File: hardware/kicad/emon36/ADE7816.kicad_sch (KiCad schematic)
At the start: 39 parts, among them J2 MJ-3523-SMT, J3 MJ-3523-SMT, J4 MJ-3523-SMT, J5 MJ-3523-SMT, J6 MJ-3523-SMT

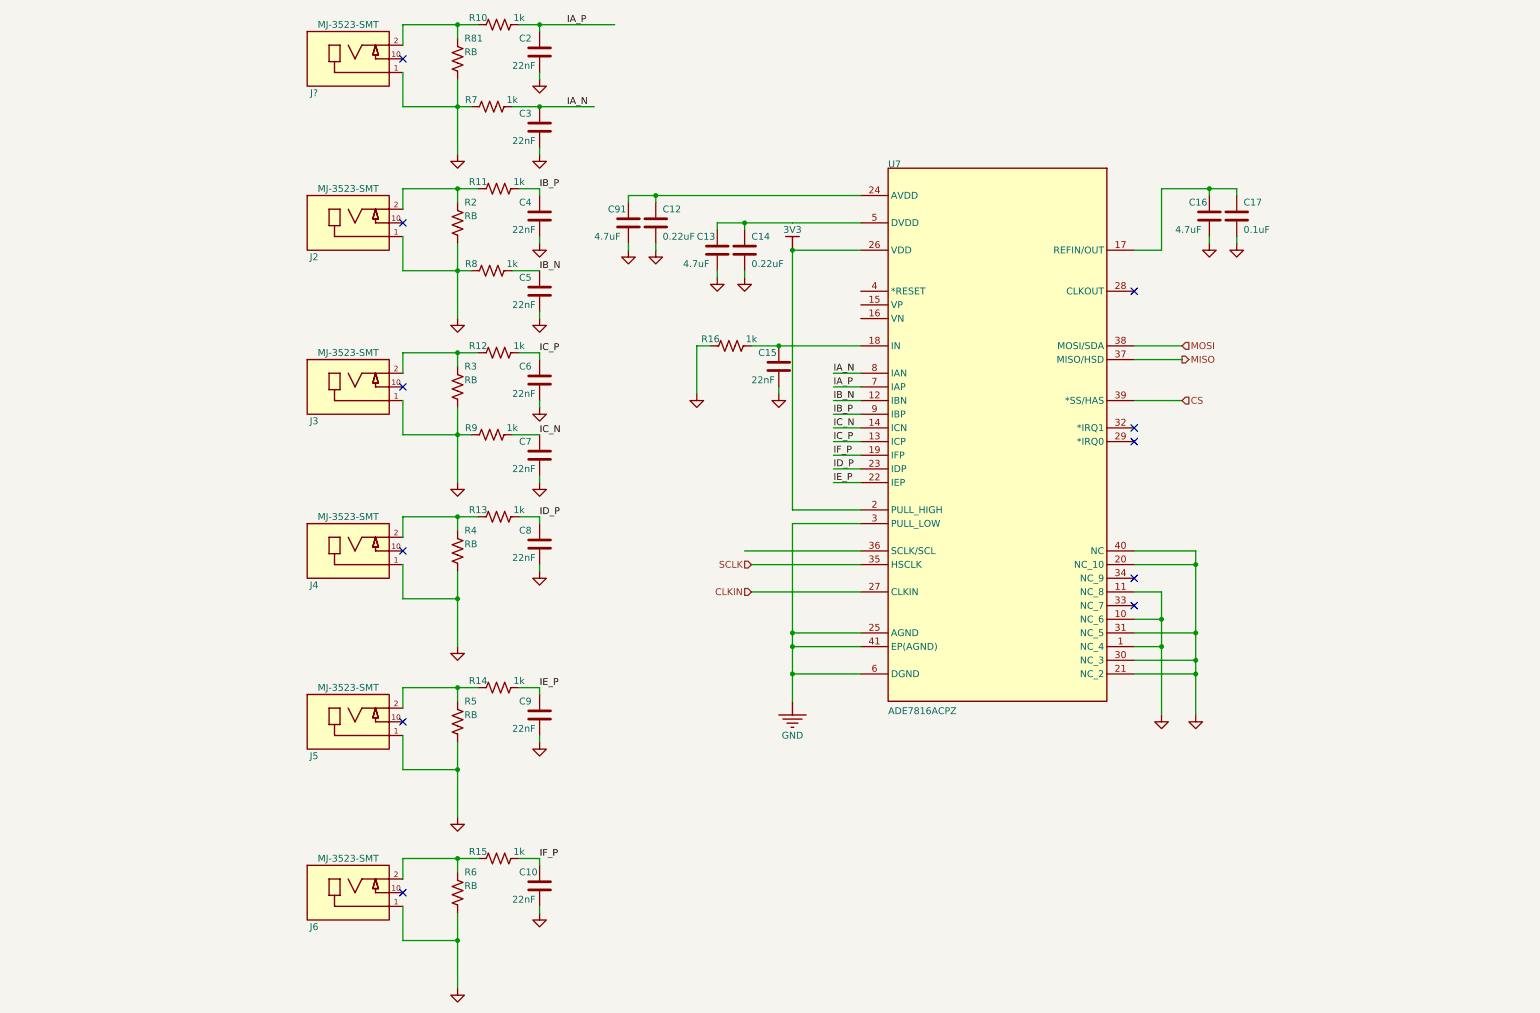
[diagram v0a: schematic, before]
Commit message: Add preliminary USB interface
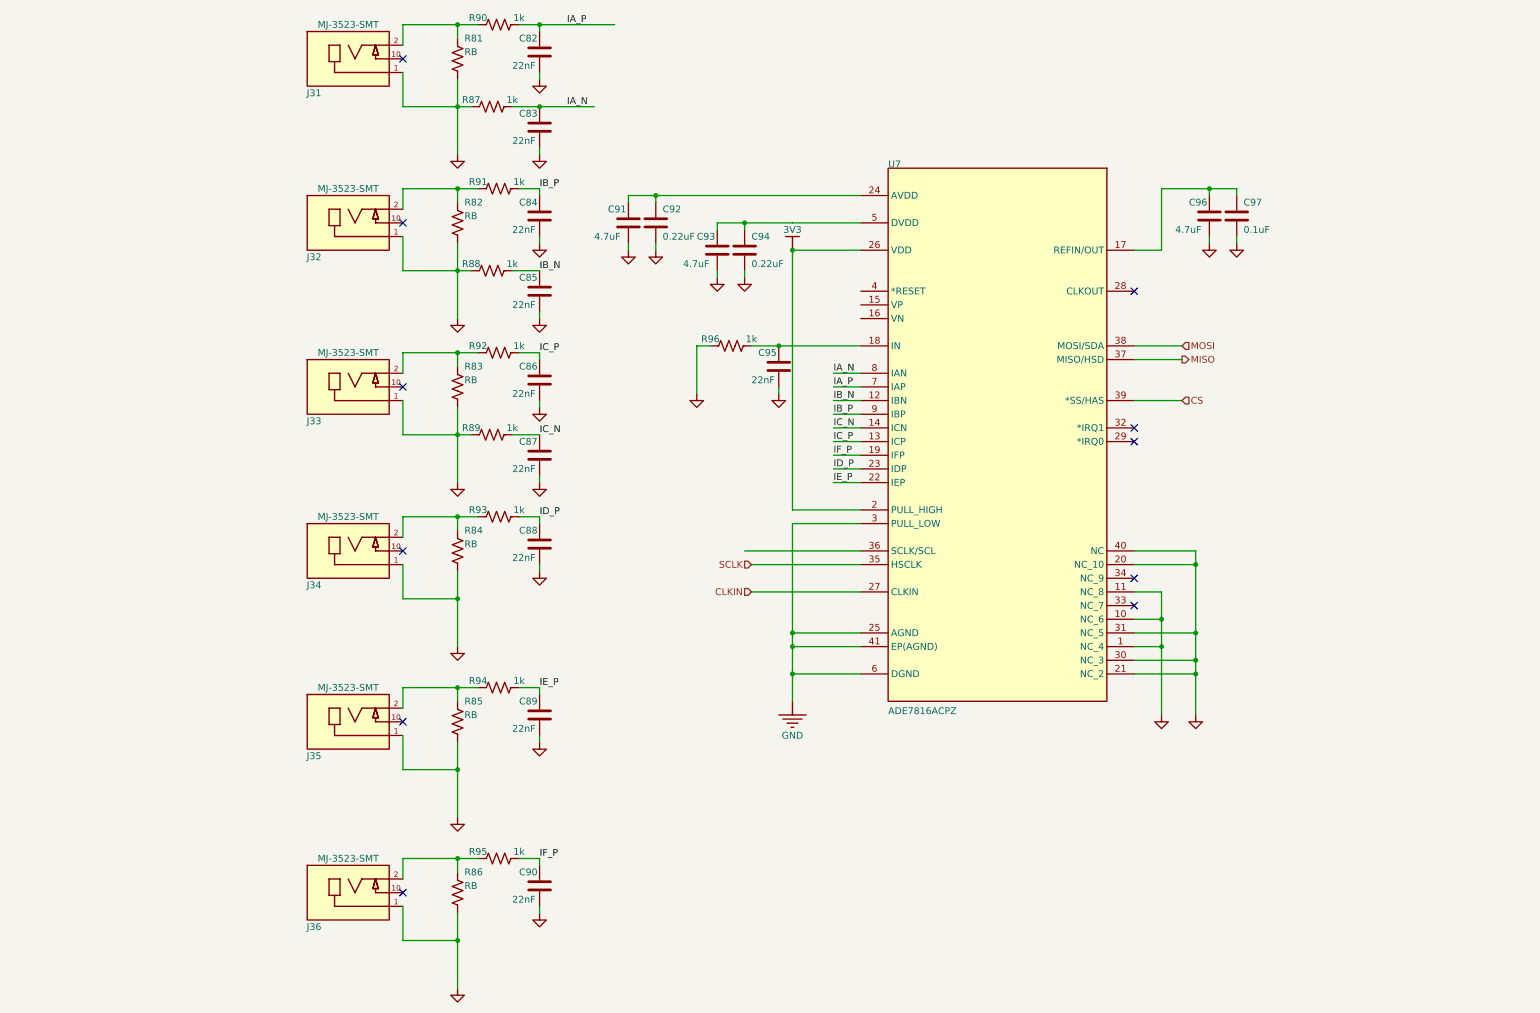
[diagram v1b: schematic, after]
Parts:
- C91: footprint (none) -> Capacitor_SMD:C_0603_1608Metric
- J31: renamed from J?; footprint CUI_MJ-3523-SMT -> emon36:CUI_MJ-3523-SMT
- J32: renamed from J2; footprint CUI_MJ-3523-SMT -> emon36:CUI_MJ-3523-SMT
- J33: renamed from J3; footprint CUI_MJ-3523-SMT -> emon36:CUI_MJ-3523-SMT
- J34: renamed from J4; footprint CUI_MJ-3523-SMT -> emon36:CUI_MJ-3523-SMT
- J35: renamed from J5; footprint CUI_MJ-3523-SMT -> emon36:CUI_MJ-3523-SMT
- J36: renamed from J6; footprint CUI_MJ-3523-SMT -> emon36:CUI_MJ-3523-SMT
- U7: footprint QFN50P600X600X75-41N-D -> emon36:QFN50P600X600X75-41N-D
- renumbered C2 to C82, C3 to C83, C4 to C84, C5 to C85, C6 to C86, C7 to C87, C8 to C88, C9 to C89, C10 to C90, C12 to C92, C13 to C93, C14 to C94, C15 to C95, C16 to C96, C17 to C97, R2 to R82, R3 to R83, R4 to R84, R5 to R85, R6 to R86, R7 to R87, R8 to R88, R9 to R89, R10 to R90, R11 to R91, R12 to R92, R13 to R93, R14 to R94, R15 to R95, R16 to R96

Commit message: Reverted to stacked 3.5mm connectors. Now has 42 channels. Added OLED, switches, power system. Cleaned up channel page.
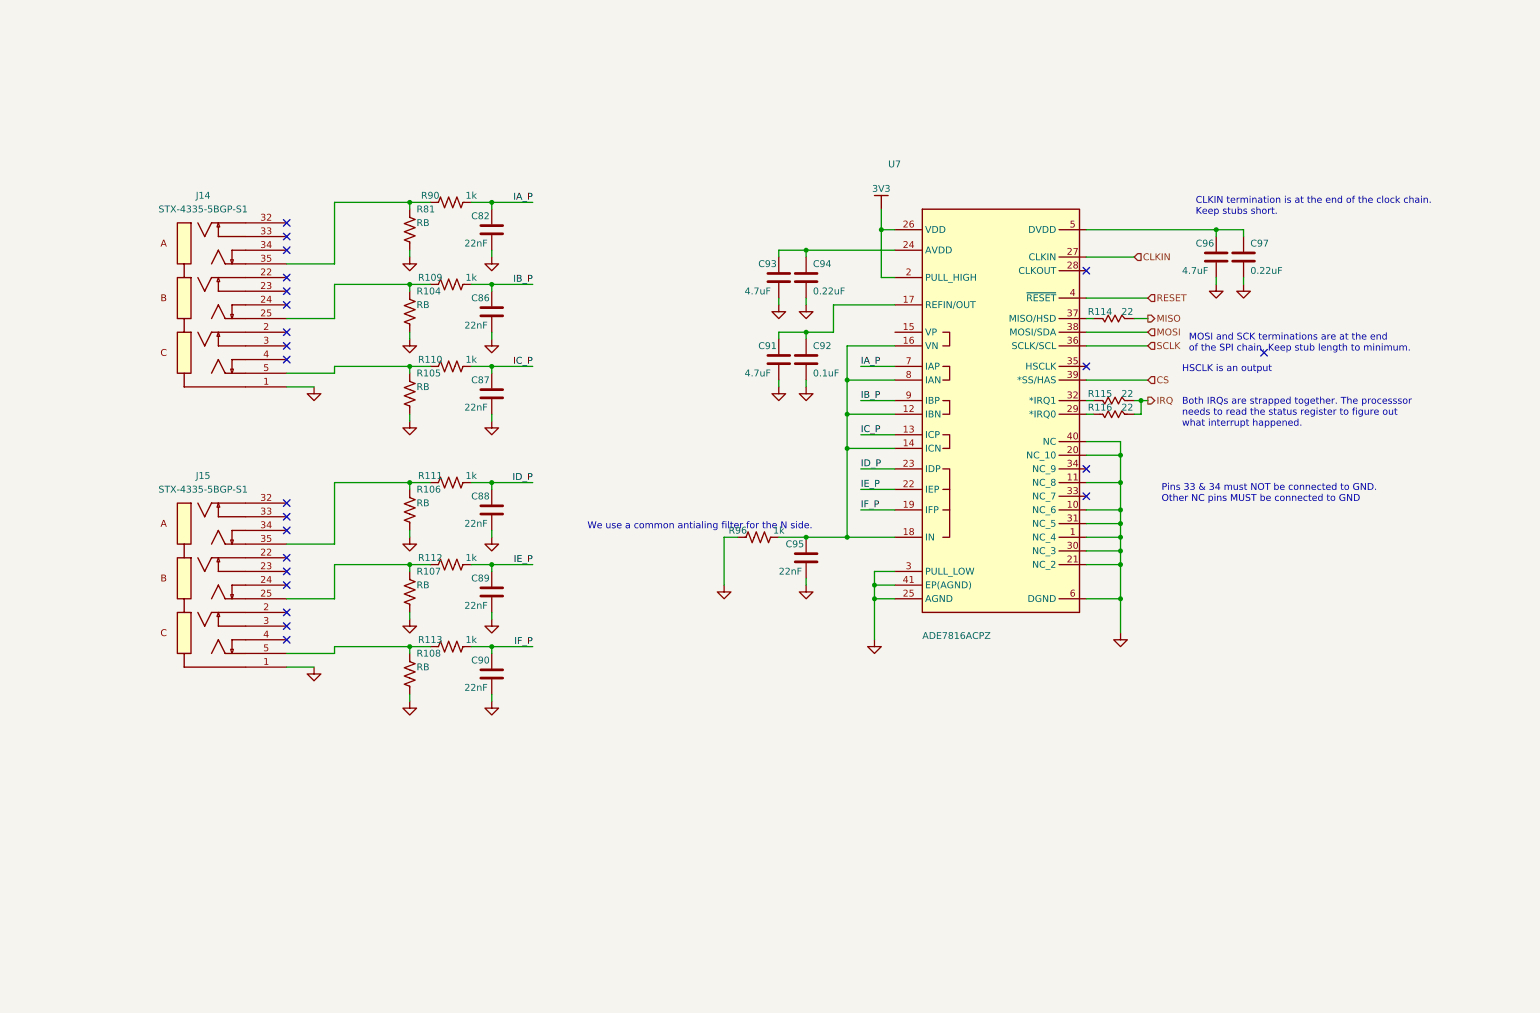
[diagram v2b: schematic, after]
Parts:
- removed C83, C84, C85: 22nF, Capacitor_SMD:C_0603_1608Metric, symbol Device:C
- removed J31, J32, J33, J34, J35, J36: MJ-3523-SMT, emon36:CUI_MJ-3523-SMT, symbol emon36:MJ-3523-SMT
- removed R82, R83, R84, R85, R86: RB, Resistor_SMD:R_0603_1608Metric, symbol Device:R_US
- removed R87, R88, R89, R91, R92, R93, R94, R95: 1k, Resistor_SMD:R_0603_1608Metric, symbol Device:R_US
- added J14, J15: STX-4335-5BGP-S1, Connector_Audio:STX-4335-5BGP-S1_KYC, symbol emon36:STX-4335-5BGP-S1
- added R104, R105, R106, R107, R108: RB, Resistor_SMD:R_0603_1608Metric, symbol Device:R_US
- added R109, R110, R111, R112, R113: 1k, Resistor_SMD:R_0603_1608Metric, symbol Device:R_US
- added R114, R115, R116: 22, Resistor_SMD:R_0603_1608Metric, symbol emon36:RES0603
- C92: value 0.22uF -> 0.1uF
- C97: value 0.1uF -> 0.22uF
- U7: symbol ADE7816-altium-import:0_ADE7816ACPZ -> emon36:ADE7816ACPZ
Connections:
- net IA_N is gone; now on an unnamed net: U7.8 (IAN)
- net IB_N is gone; now on an unnamed net: U7.12 (IBN)
- net GND: now also J14.1, J15.1, R104.2, R105.2, R106.2, R107.2, R108.2
- net IB_P: now also C86.1, R109.2
- net IC_P: now also C87.1, R110.2; no longer C86.1
- net ID_P: now also R111.2
- net IE_P: now also R112.2
- net IF_P: now also R113.2
- net MISO: now also R114.2; no longer U7.37 (MISO/HSD)
- net SCLK: now also U7.36 (SCLK/SCL); no longer U7.35 (HSCLK)
- net at C93.1, C94.1: now also U7.24 (AVDD); no longer U7.5 (DVDD)
- net at C91.1, C92.1: now also U7.17 (REFIN/OUT); no longer U7.24 (AVDD)
- net at R81.1, R90.1: now also J14.35
- net at C96.1, C97.1: now also U7.5 (DVDD); no longer U7.17 (REFIN/OUT)
- net at C95.1, R96.2, U7.18 (IN): now also U7.14 (ICN), U7.16 (VN)
- net at U7.29 (*IRQ0): now also R116.1
- net at U7.32 (*IRQ1): now also R115.1
- net RESET: now reaches U7.4 (~{RESET})
- removed net IC_N: C87.1, U7.14 (ICN)
- new net: J15.35, R106.1, R111.1
- new net: J15.25, R107.1, R112.1
- new net: J15.5, R108.1, R113.1
- new net: R114.1, U7.37 (MISO/HSD)
- new net: J14.25, R104.1, R109.1
- new net: J14.5, R105.1, R110.1
- new net IRQ: R115.2, R116.2
- no-connect marks 11 -> 23
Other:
- note added: "Both IRQs are strapped together. The processsor needs to read the status register to figure out what interrupt happened."
- note added: "CLKIN termination is at the end of the clock chain. Keep stubs short."
- note added: "HSCLK is an output"
- note added: "MOSI and SCK terminations are at the end of the SPI chain. Keep stub length to minimum."
- note added: "Pins 33 & 34 must NOT be connected to GND. Other NC pins MUST be connected to GND"
- note added: "We use a common antialing filter for the N side."
- moved on the sheet: C82, C93, C94, C95, R81, R90, R96

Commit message: Another major schematics/PCB iteration. Added decoupling caps, interrupts, etc. Improved power system. Added clock.
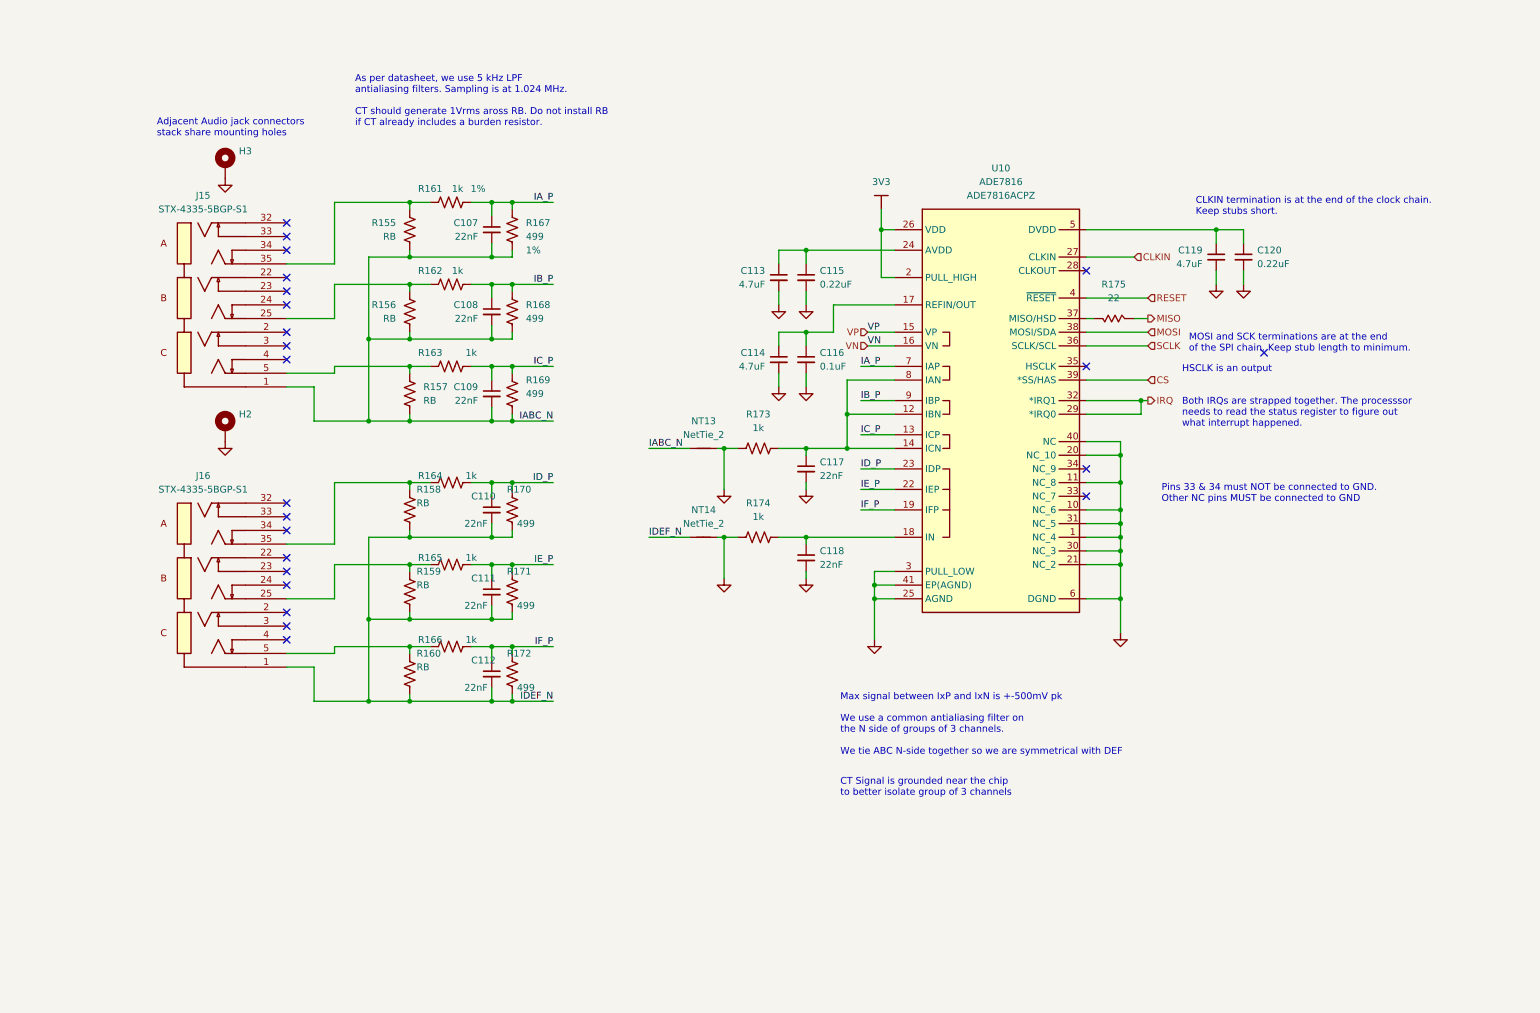
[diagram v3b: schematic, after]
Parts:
- removed R115, R116: 22, Resistor_SMD:R_0603_1608Metric, symbol emon36:RES0603
- added C117: 22nF, Capacitor_SMD:C_0603_1608Metric, symbol Device:C_Small
- added H2, H3: MountingHole_Pad, Connector_Audio_local:STX-4335_Combined_Mounting_Hole, symbol Mechanical:MountingHole_Pad
- added NT13, NT14: NetTie_2, NetTie:NetTie-2_SMD_Pad0.5mm, symbol Device:NetTie_2
- added R167, R168, R169, R170, R171, R172: 499, Resistor_SMD:R_0603_1608Metric, symbol Device:R_US
- added R173: 1k, Resistor_SMD:R_0603_1608Metric, symbol Device:R_US
- C107: renamed from C82; symbol Device:C -> Device:C_Small
- C108: renamed from C86; symbol Device:C -> Device:C_Small
- C109: renamed from C87; symbol Device:C -> Device:C_Small
- C110: renamed from C88; symbol Device:C -> Device:C_Small
- C111: renamed from C89; symbol Device:C -> Device:C_Small
- C112: renamed from C90; symbol Device:C -> Device:C_Small
- C113: renamed from C93; symbol Device:C -> Device:C_Small
- C114: renamed from C91; symbol Device:C -> Device:C_Small
- C115: renamed from C94; symbol Device:C -> Device:C_Small
- C116: renamed from C92; symbol Device:C -> Device:C_Small
- C118: renamed from C95; symbol Device:C -> Device:C_Small
- C119: renamed from C96; symbol Device:C -> Device:C_Small
- C120: renamed from C97; symbol Device:C -> Device:C_Small
- J15: renamed from J14; footprint Connector_Audio:STX-4335-5BGP-S1_KYC -> Connector_Audio_local:STX-4335-5BGP-S1_KYC; MFR (none) -> KYCON, INC.; MFR_NAME KYCON, INC. -> (none); MPN (none) -> STX-4335-5BGP-S1
- J16: renamed from J15; footprint Connector_Audio:STX-4335-5BGP-S1_KYC -> Connector_Audio_local:STX-4335-5BGP-S1_KYC; MFR (none) -> KYCON, INC.; MFR_NAME KYCON, INC. -> (none); MPN (none) -> STX-4335-5BGP-S1
- R161: renamed from R90; Tol (none) -> 1%
- U10: renamed from U7; value ~ -> ADE7816; footprint emon36:QFN50P600X600X75-41N-D -> Package_DFN_QFN:QFN-40-1EP_6x6mm_P0.5mm_EP4.6x4.6mm; MFR (none) -> Analog Devices; MPN (none) -> ADE7816ACPZ
- renumbered R81 to R155, R104 to R156, R105 to R157, R106 to R158, R107 to R159, R108 to R160, R109 to R162, R110 to R163, R111 to R164, R112 to R165, R113 to R166, R96 to R174, R114 to R175
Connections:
- net GND: now also C117.2, H2.1, H3.1, NT13.2, NT14.2, R173.1; no longer C107.2, C108.2, C109.2, C110.2, C111.2, C112.2, J15.1, J16.1, R155.2, R156.2, R157.2, R158.2, R159.2, R160.2
- net IA_P: now also R167.1
- net IB_P: now also R168.1
- net IC_P: now also R169.1
- net ID_P: now also R170.1
- net IE_P: now also R171.1
- net IF_P: now also R172.1
- net IRQ: now also U10.29 (*IRQ0), U10.32 (*IRQ1)
- net VP: now reaches U10.15 (VP)
- new net: C117.1, R173.2, U10.12 (IBN), U10.14 (ICN), U10.8 (IAN)
- new net: C118.1, R174.2, U10.18 (IN)
- new net IABC_N: C107.2, C108.2, C109.2, J15.1, NT13.1, R155.2, R156.2, R157.2, R167.2, R168.2, R169.2
- new net IDEF_N: C110.2, C111.2, C112.2, J16.1, NT14.1, R158.2, R159.2, R160.2, R170.2, R171.2, R172.2
- new net VN: U10.16 (VN)
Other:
- note added: "Adjacent Audio jack connectors stack share mounting holes"
- note added: "As per datasheet, we use 5 kHz LPF antialiasing filters. Sampling is at 1.024 MHz. CT should generate 1Vrms aross RB. Do not install RB if CT already includes a burden resistor."
- note added: "CT Signal is grounded near the chip to better isolate group of 3 channels"
- note added: "Max signal between IxP and IxN is +-500mV pk"
- note added: "We use a common antialiasing filter on the N side of groups of 3 channels. We tie ABC N-side together so we are symmetrical with DEF"
- note removed: "We use a common antialing filter for the N side."
- company: JFC Inc -> JFCInc
- title: Energy monitor channel -> EMON36 - 36-channel single-board energy monitor

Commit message: Finished schematics, layout and routing. Ready for verification.
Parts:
- removed J15, J16: STX-4335-5BGP-S1, Connector_Audio_local:STX-4335-5BGP-S1_KYC, symbol emon36:STX-4335-5BGP-S1
- removed NT13, NT14: NetTie_2, NetTie:NetTie-2_SMD_Pad0.5mm, symbol Device:NetTie_2
- added H27, H28: MountingHole_Pad, _Connector_Audio_local:STX-4335_Combined_Mounting_Hole, symbol Mechanical:MountingHole_Pad
- added J15: 6_port_3.5mm_audio_jack_array_module_left_column, _Connector_Audio_local:6_ports_3.5mm_audio_jack_array_module_left_column, symbol emon36:6_port_3.5mm_audio_jack_array_module_left_column
- added J16: 6_port_3.5mm_audio_jack_array_module_right_column, _Connector_Audio_local:6_ports_3.5mm_audio_jack_array_module_right_column, symbol emon36:6_port_3.5mm_audio_jack_array_module_right_column
- C113, C114, C119: value 4.7uF -> 4.7uF/10V; Desc (none) -> CAP CER 4.7UF 10V X7S 0603; MFR (none) -> TDK Corporation; MPN (none) -> C1608X7S1A475K080AC
- H13: renamed from H3; footprint Connector_Audio_local:STX-4335_Combined_Mounting_Hole -> _Connector_Audio_local:STX-4335_Combined_Mounting_Hole
- H14: renamed from H2; footprint Connector_Audio_local:STX-4335_Combined_Mounting_Hole -> _Connector_Audio_local:STX-4335_Combined_Mounting_Hole
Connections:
- net IABC_N is gone; now on net GND: C107.2, C108.2, C109.2, R155.2, R156.2, R157.2, R167.2, R168.2, R169.2
- net IDEF_N is gone; now on net GND: C110.2, C111.2, C112.2, R158.2, R159.2, R160.2, R170.2, R171.2, R172.2
- net GND: now also H27.1, H28.1, J15.1A, J15.24A, J15.34A, J16.1B, J16.24B, J16.34B
- net ID_P_R: now reaches R158.1, R164.1
- net ID_P_R: now also J15.35A
- net IE_P_R: now reaches R159.1, R165.1
- net IE_P_R: now also J15.25A
- net IF_P_R: now reaches R160.1, R166.1
- net IF_P_R: now also J15.5A
- net IABC_R: now reaches C117.1, R173.2, U10.12 (IBN), U10.14 (ICN), U10.8 (IAN)
- net AVDD: now reaches C113.1, C115.1, U10.24 (AVDD)
- net REF: now reaches C114.1, C116.1, U10.17 (REFIN/OUT)
- net MISO_R: now reaches R175.1, U10.37 (MISO/HSD)
- net IB_P_R: now reaches R156.1, R162.1
- net IB_P_R: now also J16.25B
- net IDEF_R: now reaches C118.1, R174.2, U10.18 (IN)
- net DVDD: now reaches C119.1, C120.1, U10.5 (DVDD)
- net IA_P_R: now reaches R155.1, R161.1
- net IA_P_R: now also J16.35B
- net IC_P_R: now reaches R157.1, R163.1
- net IC_P_R: now also J16.5B
- no-connect marks 23 -> 21
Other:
- moved on the sheet: H13, H14
